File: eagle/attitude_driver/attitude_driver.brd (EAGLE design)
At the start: 90 x 90 mm, 28 parts, among them J1 BT-HC06, J10 ESC2-POWER, J11 ESC3-POWER, J12 SOURCE-POWER, J13 HALL-POWER, J14 PROGRAM, J17 CURRENT-SENSOR, J2 mpu9250, J3 ESC1-PWM, J4 ESC2-PWM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

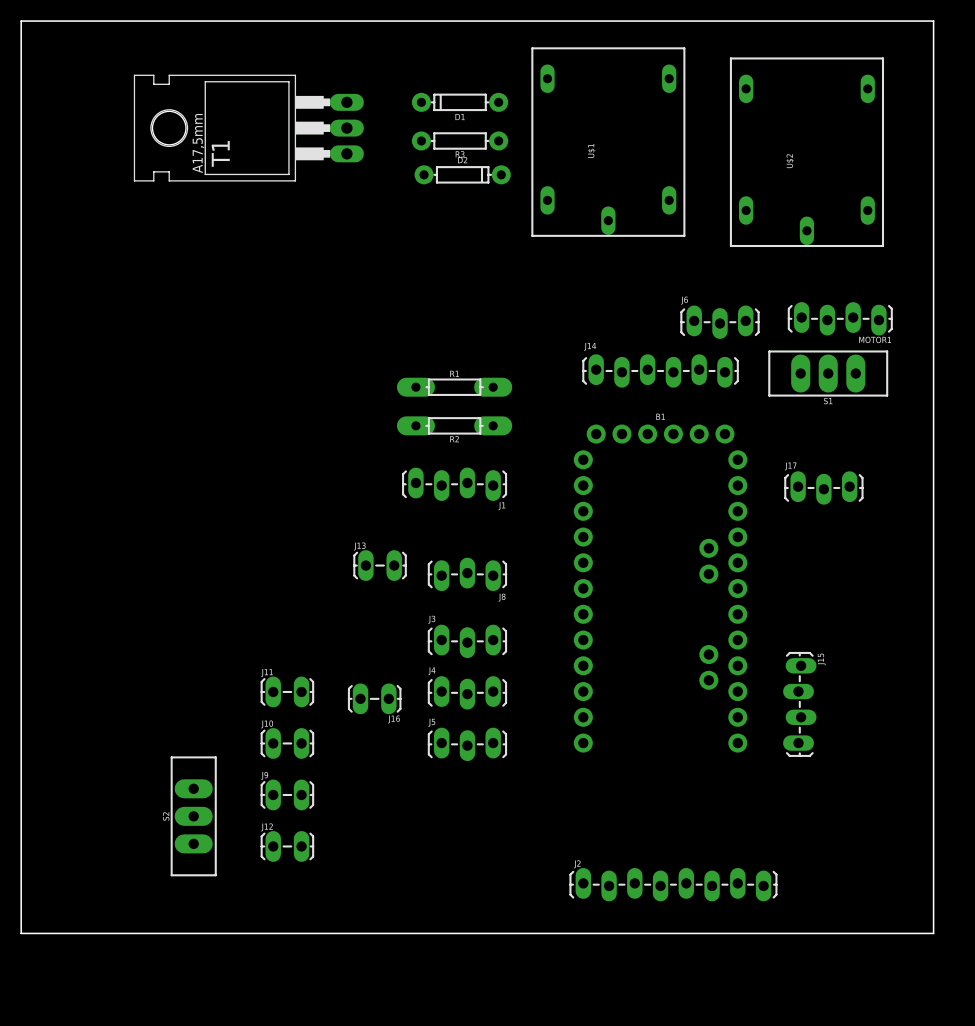
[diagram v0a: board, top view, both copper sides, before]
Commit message: ordered components
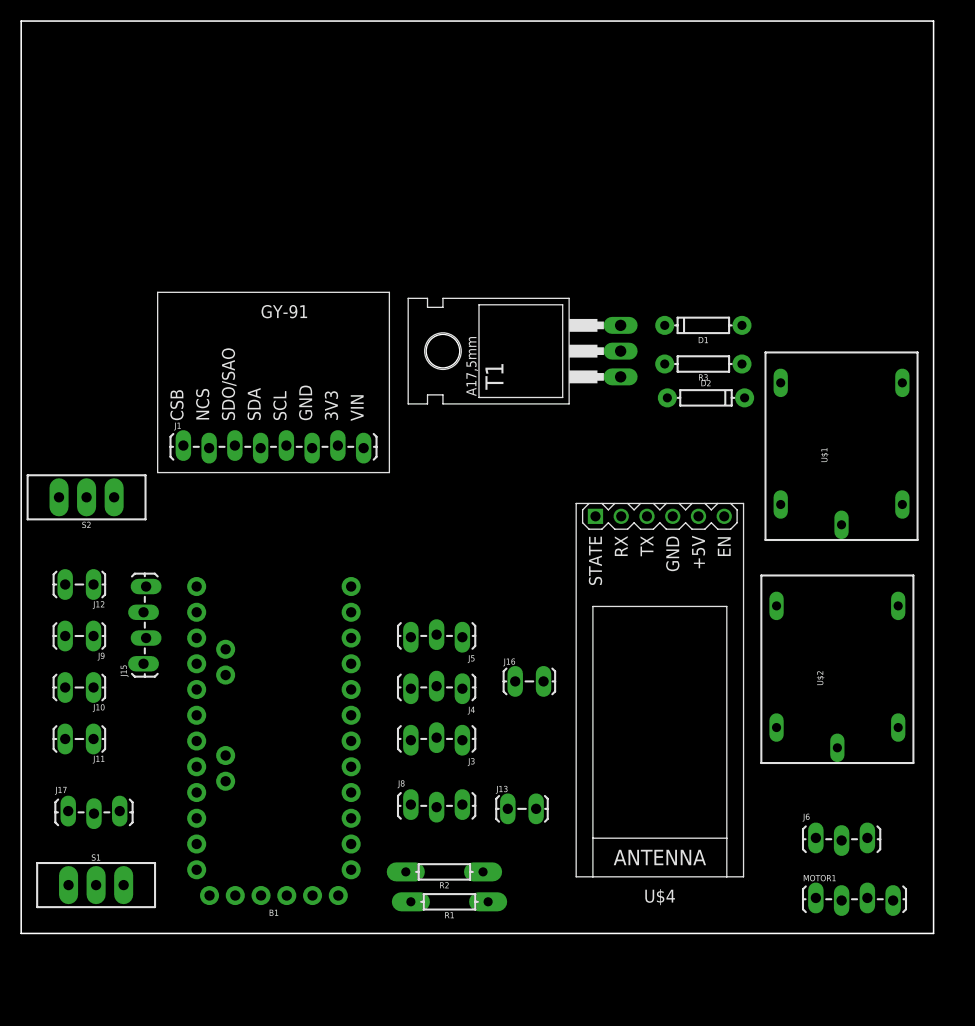
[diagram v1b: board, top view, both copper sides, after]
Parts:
- removed J14: PROGRAM, SparkFun-Connectors:1X06_LOCK_LONGPADS
- removed J2: mpu9250, SparkFun-Connectors:1X08_LOCK_LONGPADS
- added U$4: WIRELESS-BLUETOOTH-HC-05-MIRRORMIRROR, diy-modules:WIRELESS-BLUETOOTH-HC-05-MIRROR
- J1: value BT-HC06 -> (none); device SparkFun-Connectors:1X04_LOCK_LONGPADS -> gy-91:GY91_LONGPADS
- moved S1 88.1 mm to (7.39, 4.77), turned to 270 degrees
- moved J17 78.8 mm to (4.64, 12.1)
- moved J15 64.9 mm to (12.1, 26.6), turned to 90 degrees
- moved MOTOR1 57.3 mm to (78.4, 3.50), turned to 0 degrees
- moved J6 52.4 mm to (78.4, 9.42)
- moved U$2 51.1 mm to (80.4, 25.7)
- moved R1 50.8 mm to (42.2, 3.12), turned to 180 degrees
- moved R2 44.0 mm to (41.8, 6.07)
- moved B1 41.0 mm to (24.9, 19.0), turned to 180 degrees
- moved U$1 37.8 mm to (80.8, 47.7)
- moved T1 34.8 mm to (52.8, 57.4)
- moved S2 33.2 mm to (6.45, 43.0), turned to 90 degrees
- moved D1 32.6 mm to (67.3, 60.0)
- moved R3 32.6 mm to (67.3, 56.2)
- moved D2 32.6 mm to (67.5, 52.8)
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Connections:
- net 3V3: now also J1.7; no longer J2.7
- net CSB: now also J1.1; no longer J2.1
- net ESC1-5V: now also J1.8, U$4.5; no longer J1.4, J2.8
- net GND: now also J1.6, U$4.4; no longer J1.3, J14.1, J14.2, J2.6
- net N$1: now also U$4.2; no longer J1.1
- net NCS: now also J1.2; no longer J2.2
- net PROG-5V: no longer J14.3
- net RST: no longer J14.6
- net RX: now also U$4.3; no longer J1.2, J14.4
- net SAO: now also J1.3; no longer J2.3
- net SCL: now also J1.5; no longer J2.5
- net SDA: now also J1.4; no longer J2.4
- net TX: no longer J14.5

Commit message: update pcb design
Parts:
- moved J16 18.0 mm to (42.9, 41.9)
- moved J8 6.25 mm to (43.6, 16.3), turned to 180 degrees
- moved J3 5.00 mm to (43.5, 24.1)
- moved J4 5.00 mm to (43.5, 29.1)
- moved J5 5.00 mm to (43.5, 34.2)
- moved J13 4.00 mm to (48.1, 16.3)
- moved S2 2.34 mm to (8.55, 42.0), turned to 270 degrees
- moved S1 2.00 mm to (9.39, 4.77)
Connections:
- new net N$4: D1.C, T1.3, U$1.COIL0, U$2.COIL1
- net ESC2-5V: no longer J16.1
- net ESC3-5V: now also J16.1
- net GND: no longer D1.C, T1.3, U$1.COIL0, U$2.COIL1
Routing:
- net GND: track 0.00 -> 385.7 mm, vias 0 -> 8
- net ESC1-5V: track 0.00 -> 205.4 mm, vias 0 -> 2
- net N$4: track 0.00 -> 102.3 mm, vias 0 -> 2
- net M1-DIR: track 0.00 -> 68.4 mm, vias 0 -> 2
- net NCS: track 0.00 -> 65.3 mm, vias 0 -> 2
- net H3: track 0.00 -> 59.8 mm, vias 0 -> 2
- net N$1: track 0.00 -> 59.7 mm, vias 0 -> 2
- net M1A: track 0.00 -> 57.0 mm
- net M1C: track 0.00 -> 56.7 mm
- net SAO: track 0.00 -> 51.5 mm, vias 0 -> 4
- net RX: track 0.00 -> 50.9 mm
- net SCL: track 0.00 -> 38.0 mm
- net CSB: track 0.00 -> 35.7 mm, vias 0 -> 2
- net SDA: track 0.00 -> 32.9 mm
- net ESC1A: track 0.00 -> 32.3 mm
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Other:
- board size 90 x 90 mm -> 92 x 76 mm
